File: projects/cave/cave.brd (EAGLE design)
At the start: 100 x 72 mm, 111 parts, among them U1 IRLML6344TRPBF, U10 IRLML6344TRPBF, U11 IRLML6344TRPBF, U12 IRLML6344TRPBF, U2 TLC555CDR, U3 IRLML6344TRPBF, U4 IRLML6344TRPBF, U5 IRLML6344TRPBF, U6 IRLML6344TRPBF, U7 TPS54625, U9 IRLML6344TRPBF

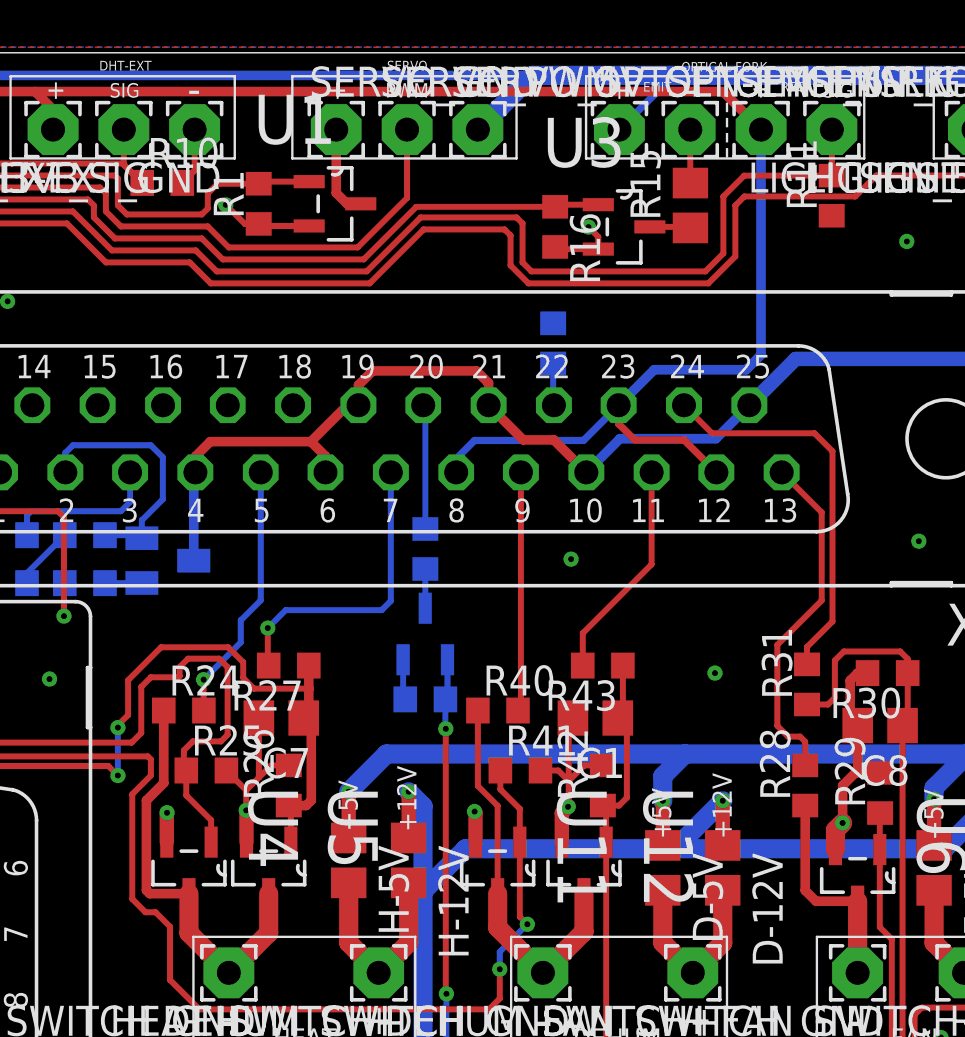
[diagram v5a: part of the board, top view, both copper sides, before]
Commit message: Changed 250ohm-0603 led res to 255ohm-0805. Generated BOM
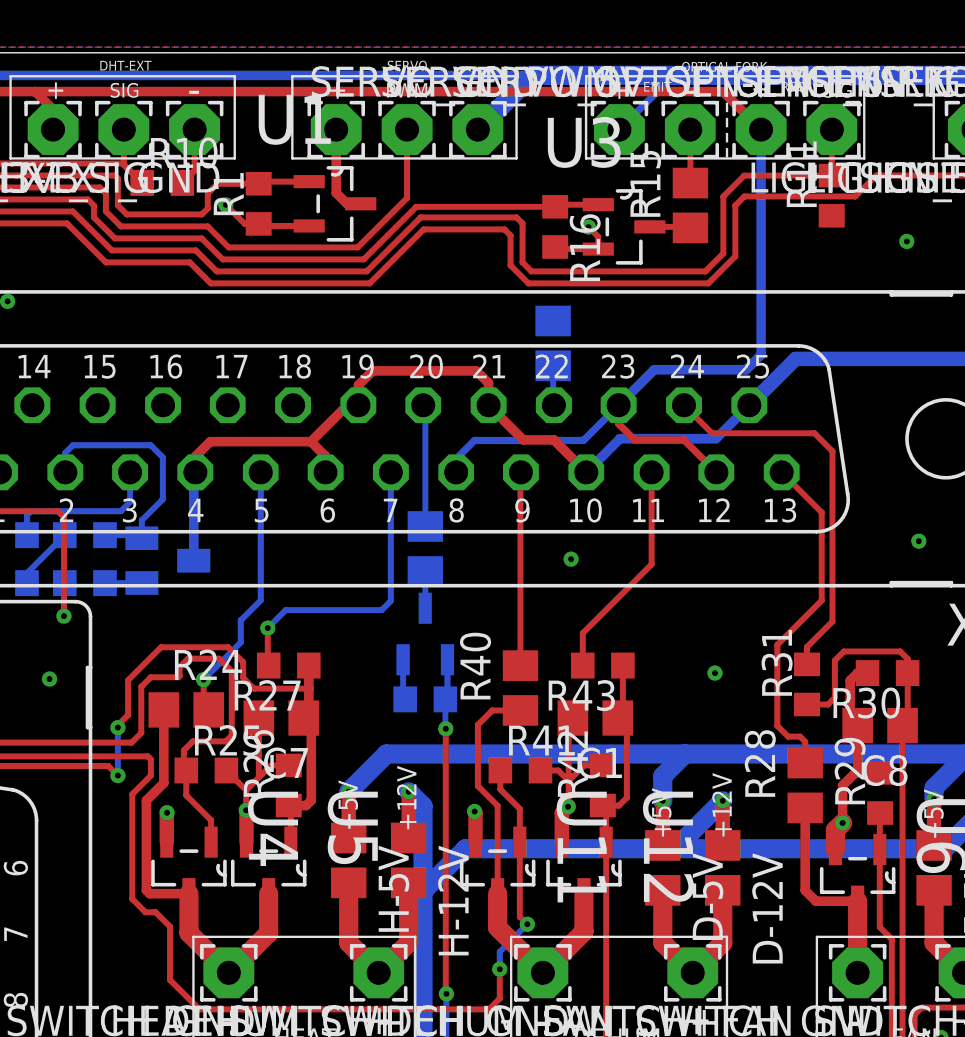
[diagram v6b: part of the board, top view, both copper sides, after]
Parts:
- R24, R28, R36, R38, R40: value 250 -> 255; device rcl:R0603 -> rcl:R0805
- R32: value 100k 1% -> 100k
- moved R40 1.35 mm to (41.5, 45.1), turned to 90 degrees
- moved R24 0.10 mm to (27.4, 44.2)
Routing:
- net DEHUM_LED: track 10.1 -> 8.20 mm
- net N$24: track 16.5 -> 17.8 mm

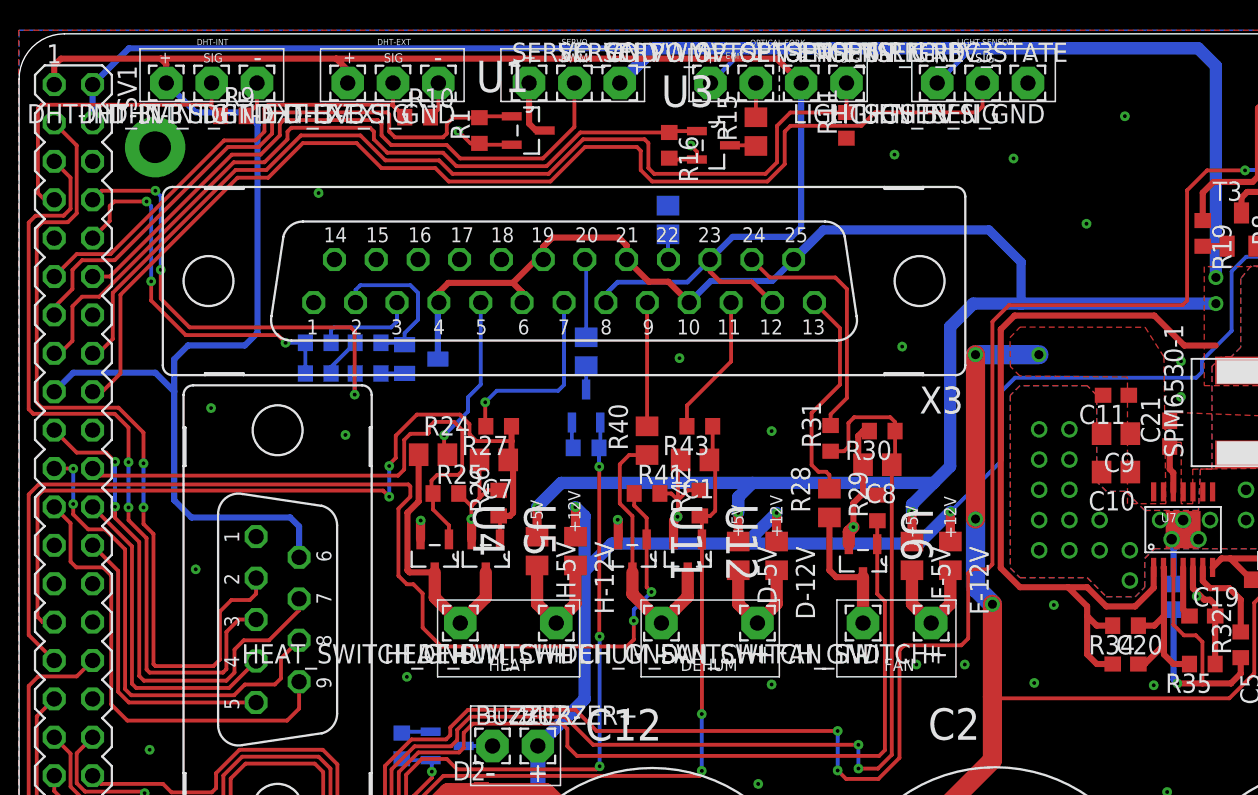
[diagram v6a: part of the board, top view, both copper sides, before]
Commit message: Reset lever circuit added to schematic and board ! BOM updated.
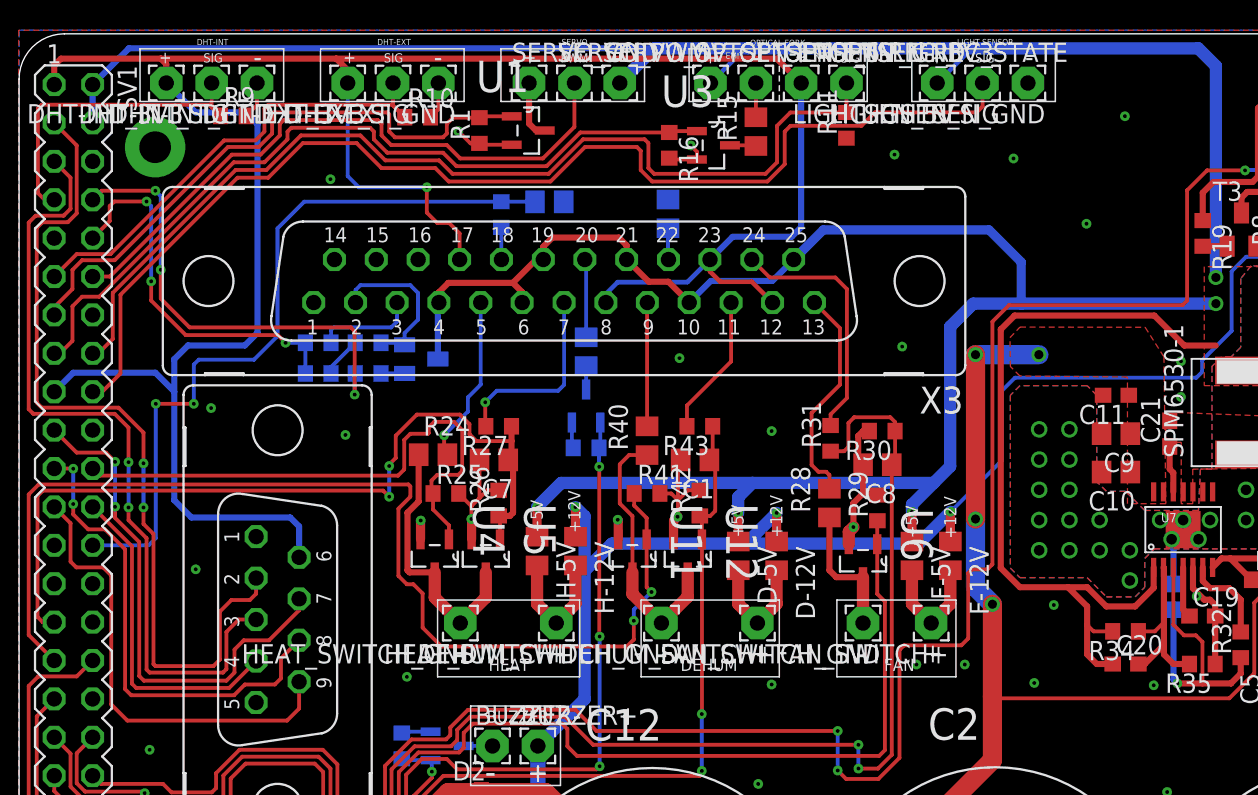
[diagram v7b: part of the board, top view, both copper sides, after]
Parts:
- added C4: 10uF/25V, rcl:C0805
- added R5: 4.7k, rcl:R0603
- moved R36 0.41 mm to (42.9, 60.1)
- moved R34 0.38 mm to (73.2, 32.5)
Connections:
- removed net SPI_CE1: SV1.26, X2.5
- new net RESET_LEVER_F: C4.1, R5.1, SV1.26
- new net RESET_LEVER_IN: R5.2, X3.18
- net +3V3: now also X3.17
- net GND: now also C4.2, X2.5; no longer X3.17, X3.18
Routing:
- net RESET_LEVER_F: track 0.00 -> 49.6 mm, vias 0 -> 2
- net SPI_CE1: track 19.8 -> 0.00 mm
- net +3V3: track 142.4 -> 160.2 mm, vias 0 -> 1
- net RESET_LEVER_IN: track 0.00 -> 2.13 mm
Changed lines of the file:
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@@
 <element name="R30" library="rcl" package="R0603" value="100k" x="57.0985" y="45.7192" rot="R180"/>
 <element name="R31" library="rcl" package="R0603" value="4.7k" x="53.6836" y="45.2382" rot="R90"/>
-<element name="R36" library="rcl" package="R0805" value="255" x="42.92728125" y="59.68708125" rot="MR270"/>
+<element name="R36" library="rcl" package="R0805" value="255" x="42.92728125" y="60.09348125" rot="MR270"/>
 <element name="R37" library="rcl" package="R0603" value="10k" x="37.5109" y="44.60851875" rot="MR0"/>
 <element name="R38" library="rcl" package="R0805" value="255" x="37.5109" y="50.9763" rot="MR90"/>
@@
 <element name="R32" library="rcl" package="R0603" value="100k" x="80.8156" y="31.5807" rot="R90"/>
 <element name="C19" library="rcl" package="C0603" value="8200pF/50V" x="78.2756" y="33.4857"/>
-<element name="R34" library="rcl" package="R0603" value="124k 1%" x="73.1956" y="32.8507" rot="R180"/>
+<element name="R34" library="rcl" package="R0603" value="124k 1%" x="73.1956" y="32.4697" rot="R180"/>
 <element name="R35" library="rcl" package="R0603" value="22.1k 1%" x="78.2756" y="30.3107" rot="R180"/>
 <element name="C20" library="rcl" package="C0603" value="10pF/50V" x="73.1956" y="30.3107"/>
@@
 <attribute name="MPN" value="" x="36.0506" y="55.6455" size="1.778" layer="27" rot="R180" display="off"/>
 </element>
+<element name="R5" library="rcl" package="R0603" value="4.7k" x="31.9024" y="60.0456" rot="MR270"/>
+<element name="C4" library="rcl" package="C0805" value="10uF/25V" x="35.0774" y="60.8838" rot="MR180"/>
 </elements>
 <signals>
@@
 <contactref element="C3" pad="2"/>
 <contactref element="X3" pad="1"/>
-<contactref element="X3" pad="18"/>
-<contactref element="X3" pad="17"/>
 <contactref element="X3" pad="16"/>
 <contactref element="X3" pad="15"/>
@@
 <via x="43.688" y="50.546" extent="1-16" drill="0.25"/>
 <via x="58.42" y="51.308" extent="1-16" drill="0.25"/>
-<via x="19.812" y="61.468" extent="1-16" drill="0.25"/>
+<via x="20.5994" y="62.3824" extent="1-16" drill="0.25"/>
 <via x="12.7" y="47.244" extent="1-16" drill="0.25"/>
 <via x="21.59" y="45.466" extent="1-16" drill="0.25"/>
@@
 <wire x1="43.2936" y1="38.5564" x2="43.2936" y2="39.7884" width="0.6096" layer="1"/>
 <wire x1="43.2936" y1="39.7884" x2="43.561" y2="40.0558" width="0.6096" layer="1"/>
+<contactref element="X2" pad="5"/>
+<contactref element="C4" pad="2"/>
 </signal>
 <signal name="DHT22_EXT">
@@
 <wire x1="13.897440625" y1="28.7274" x2="15.6797" y2="30.509659375" width="0.254" layer="1"/>
 </signal>
-<signal name="SPI_CE1">
+<signal name="RESET_LEVER_F">
 <contactref element="SV1" pad="26"/>
-<contactref element="X2" pad="5"/>
-<wire x1="4.8641" y1="38.1635" x2="6.5532" y2="36.4744" width="0.254" layer="1"/>
-<wire x1="6.5532" y1="36.4744" x2="6.5532" y2="28.4734" width="0.254" layer="1"/>
-<wire x1="6.5532" y1="28.4734" x2="7.260140625" y2="27.766459375" width="0.254" layer="1"/>
-<wire x1="7.260140625" y1="27.766459375" x2="15.6797" y2="27.766459375" width="0.254" layer="1"/>
+<contactref element="R5" pad="1"/>
+<contactref element="C4" pad="1"/>
+<wire x1="31.9024" y1="60.8956" x2="34.1156" y2="60.8956" width="0.254" layer="16"/>
+<wire x1="34.1156" y1="60.8956" x2="34.1274" y2="60.8838" width="0.254" layer="16"/>
+<wire x1="4.8641" y1="38.1635" x2="8.5725" y2="38.1635" width="0.254" layer="16"/>
+<wire x1="8.5725" y1="38.1635" x2="9.0424" y2="38.6334" width="0.254" layer="16"/>
+<wire x1="9.0424" y1="38.6334" x2="9.0424" y2="47.5234" width="0.254" layer="16"/>
+<via x="9.0424" y="47.5234" extent="1-16" drill="0.25"/>
+<wire x1="9.0424" y1="47.5234" x2="11.557" y2="47.5234" width="0.254" layer="1"/>
+<via x="11.557" y="47.5234" extent="1-16" drill="0.25"/>
+<wire x1="11.557" y1="47.5234" x2="11.557" y2="50.1142" width="0.254" layer="16"/>
+<wire x1="11.557" y1="50.1142" x2="11.8872" y2="50.4444" width="0.254" layer="16"/>
+<wire x1="11.8872" y1="50.4444" x2="15.5448" y2="50.4444" width="0.254" layer="16"/>
+<wire x1="15.5448" y1="50.4444" x2="17.0942" y2="51.9938" width="0.254" layer="16"/>
+<wire x1="17.0942" y1="51.9938" x2="17.0942" y2="59.1312" width="0.254" layer="16"/>
+<wire x1="17.0942" y1="59.1312" x2="18.8586" y2="60.8956" width="0.254" layer="16"/>
+<wire x1="18.8586" y1="60.8956" x2="31.9024" y2="60.8956" width="0.254" layer="16"/>
 </signal>
 <signal name="EEPROM_SC">
@@
 <wire x1="14.986" y1="66.802" x2="11.6806" y2="66.802" width="0.4064" layer="16"/>
 <wire x1="11.6806" y1="66.802" x2="9.7366" y2="68.746" width="0.4064" layer="16"/>
+<contactref element="X3" pad="17"/>
+<wire x1="21.7366" y1="68.746" x2="21.7366" y2="62.5914" width="0.254" layer="16"/>
+<wire x1="21.7366" y1="62.5914" x2="22.479" y2="61.849" width="0.254" layer="16"/>
+<wire x1="22.479" y1="61.849" x2="26.9748" y2="61.849" width="0.254" layer="16"/>
+<via x="26.9748" y="61.849" extent="1-16" drill="0.25"/>
+<wire x1="26.9748" y1="61.849" x2="26.9748" y2="60.1726" width="0.254" layer="1"/>
+<wire x1="26.9748" y1="60.1726" x2="27.6606" y2="59.4868" width="0.254" layer="1"/>
+<wire x1="27.6606" y1="59.4868" x2="28.448" y2="59.4868" width="0.254" layer="1"/>
+<wire x1="28.448" y1="59.4868" x2="29.1418" y2="58.793" width="0.254" layer="1"/>
+<wire x1="29.1418" y1="58.793" x2="29.1418" y2="57.0679" width="0.254" layer="1"/>
 </signal>
 <signal name="I2C_SDA">
@@
 <contactref element="R24" pad="2"/>
 <contactref element="X3" pad="5"/>
-<wire x1="28.1178" y1="44.1449" x2="28.1178" y2="45.4406" width="0.254" layer="1"/>
 <via x="28.1178" y="45.4406" extent="1-16" drill="0.25"/>
 <wire x1="28.1178" y1="45.4406" x2="29.6926" y2="47.0154" width="0.254" layer="16"/>
@@
 <wire x1="29.6926" y1="47.9552" x2="30.5388" y2="48.8014" width="0.254" layer="16"/>
 <wire x1="30.5388" y1="48.8014" x2="30.5388" y2="54.2231" width="0.254" layer="16"/>
-<wire x1="28.1178" y1="44.1449" x2="28.3326" y2="44.1571" width="0" layer="19" extent="1-1"/>
+<wire x1="28.1178" y1="45.4406" x2="28.1178" y2="44.3719" width="0.254" layer="1"/>
+<wire x1="28.1178" y1="44.3719" x2="28.3326" y2="44.1571" width="0.254" layer="1"/>
 </signal>
 <signal name="HEAT_LEVER_IN">
@@
 <contactref element="R36" pad="2"/>
 <contactref element="X3" pad="22"/>
-<wire x1="42.92728125" y1="58.73708125" x2="42.92728125" y2="57.10001875" width="0.254" layer="16"/>
+<wire x1="42.92728125" y1="59.14348125" x2="42.92728125" y2="57.10001875" width="0.254" layer="16"/>
 <wire x1="42.92728125" y1="57.10001875" x2="42.9594" y2="57.0679" width="0.254" layer="16"/>
 </signal>
@@
 <wire x1="72.3456" y1="30.3107" x2="71.2906" y2="30.3107" width="0.4064" layer="1"/>
 <wire x1="71.2906" y1="30.3107" x2="70.6556" y2="30.9457" width="0.4064" layer="1"/>
-<wire x1="70.6556" y1="30.9457" x2="70.6556" y2="33.4857" width="0.4064" layer="1"/>
-<wire x1="70.6556" y1="33.4857" x2="70.6556" y2="34.1207" width="0.4064" layer="1"/>
+<wire x1="70.6556" y1="30.9457" x2="70.6556" y2="32.893" width="0.4064" layer="1"/>
+<wire x1="70.6556" y1="32.893" x2="70.6556" y2="34.1207" width="0.4064" layer="1"/>
 <wire x1="70.6556" y1="34.1207" x2="69.3856" y2="35.3907" width="0.4064" layer="1"/>
-<wire x1="72.3456" y1="32.8507" x2="71.2906" y2="32.8507" width="0.4064" layer="1"/>
-<wire x1="71.2906" y1="32.8507" x2="70.6556" y2="33.4857" width="0.4064" layer="1"/>
 <wire x1="64.9406" y1="36.6607" x2="64.9406" y2="52.4468" width="0.4064" layer="1"/>
 <wire x1="64.9406" y1="52.4468" x2="65.855" y2="53.3612" width="0.4064" layer="1"/>
@@
 <wire x1="64.1604" y1="59.0296" x2="53.2015" y2="59.0296" width="0.6096" layer="16"/>
 <wire x1="53.2015" y1="59.0296" x2="51.2398" y2="57.0679" width="0.6096" layer="16"/>
+<wire x1="72.3456" y1="32.4697" x2="71.0789" y2="32.4697" width="0.254" layer="1"/>
+<wire x1="71.0789" y1="32.4697" x2="70.6556" y2="32.893" width="0.254" layer="1"/>
 </signal>
 <signal name="VCOND">
@@
 <wire x1="76.3706" y1="30.3107" x2="75.7356" y2="30.9457" width="0.4064" layer="1"/>
 <wire x1="75.7356" y1="30.9457" x2="75.7356" y2="31.5807" width="0.4064" layer="1"/>
-<wire x1="75.7356" y1="31.5807" x2="75.7356" y2="33.4857" width="0.4064" layer="1"/>
-<wire x1="75.7356" y1="33.4857" x2="75.7356" y2="36.6707" width="0.4064" layer="1"/>
+<wire x1="75.7356" y1="31.5807" x2="75.7356" y2="33.0708" width="0.4064" layer="1"/>
+<wire x1="75.7356" y1="33.0708" x2="75.7356" y2="36.6707" width="0.4064" layer="1"/>
 <wire x1="75.7356" y1="36.6707" x2="75.7056" y2="36.7007" width="0.4064" layer="1"/>
 <wire x1="74.0456" y1="30.3107" x2="74.4656" y2="30.3107" width="0.4064" layer="1"/>
 <wire x1="74.4656" y1="30.3107" x2="75.7356" y2="31.5807" width="0.4064" layer="1"/>
-<wire x1="74.0456" y1="32.8507" x2="75.1006" y2="32.8507" width="0.4064" layer="1"/>
-<wire x1="75.1006" y1="32.8507" x2="75.7356" y2="33.4857" width="0.4064" layer="1"/>
+<wire x1="74.0456" y1="32.4697" x2="75.1345" y2="32.4697" width="0.254" layer="1"/>
+<wire x1="75.1345" y1="32.4697" x2="75.7356" y2="33.0708" width="0.254" layer="1"/>
 </signal>
 <signal name="N$35">
@@
 <signal name="N$39">
 </signal>
+<signal name="RESET_LEVER_IN">
+<contactref element="X3" pad="18"/>
+<contactref element="R5" pad="2"/>
+<wire x1="31.9104" y1="57.0679" x2="31.9024" y2="57.0759" width="0.254" layer="16"/>
+<wire x1="31.9024" y1="57.0759" x2="31.9024" y2="59.1956" width="0.254" layer="16"/>
+</signal>
 </signals>
